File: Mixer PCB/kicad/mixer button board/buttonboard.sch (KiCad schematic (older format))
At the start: 51 parts, among them J1 Conn_01x02, J2 Conn_02x13_Odd_Even, J3 Conn_01x11, sw1 cherry_sk6812, sw10 cherry_sk6812, sw11 cherry_sk6812, sw12 cherry_sk6812, sw13 cherry_sk6812, sw14 cherry_sk6812, sw15 cherry_sk6812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

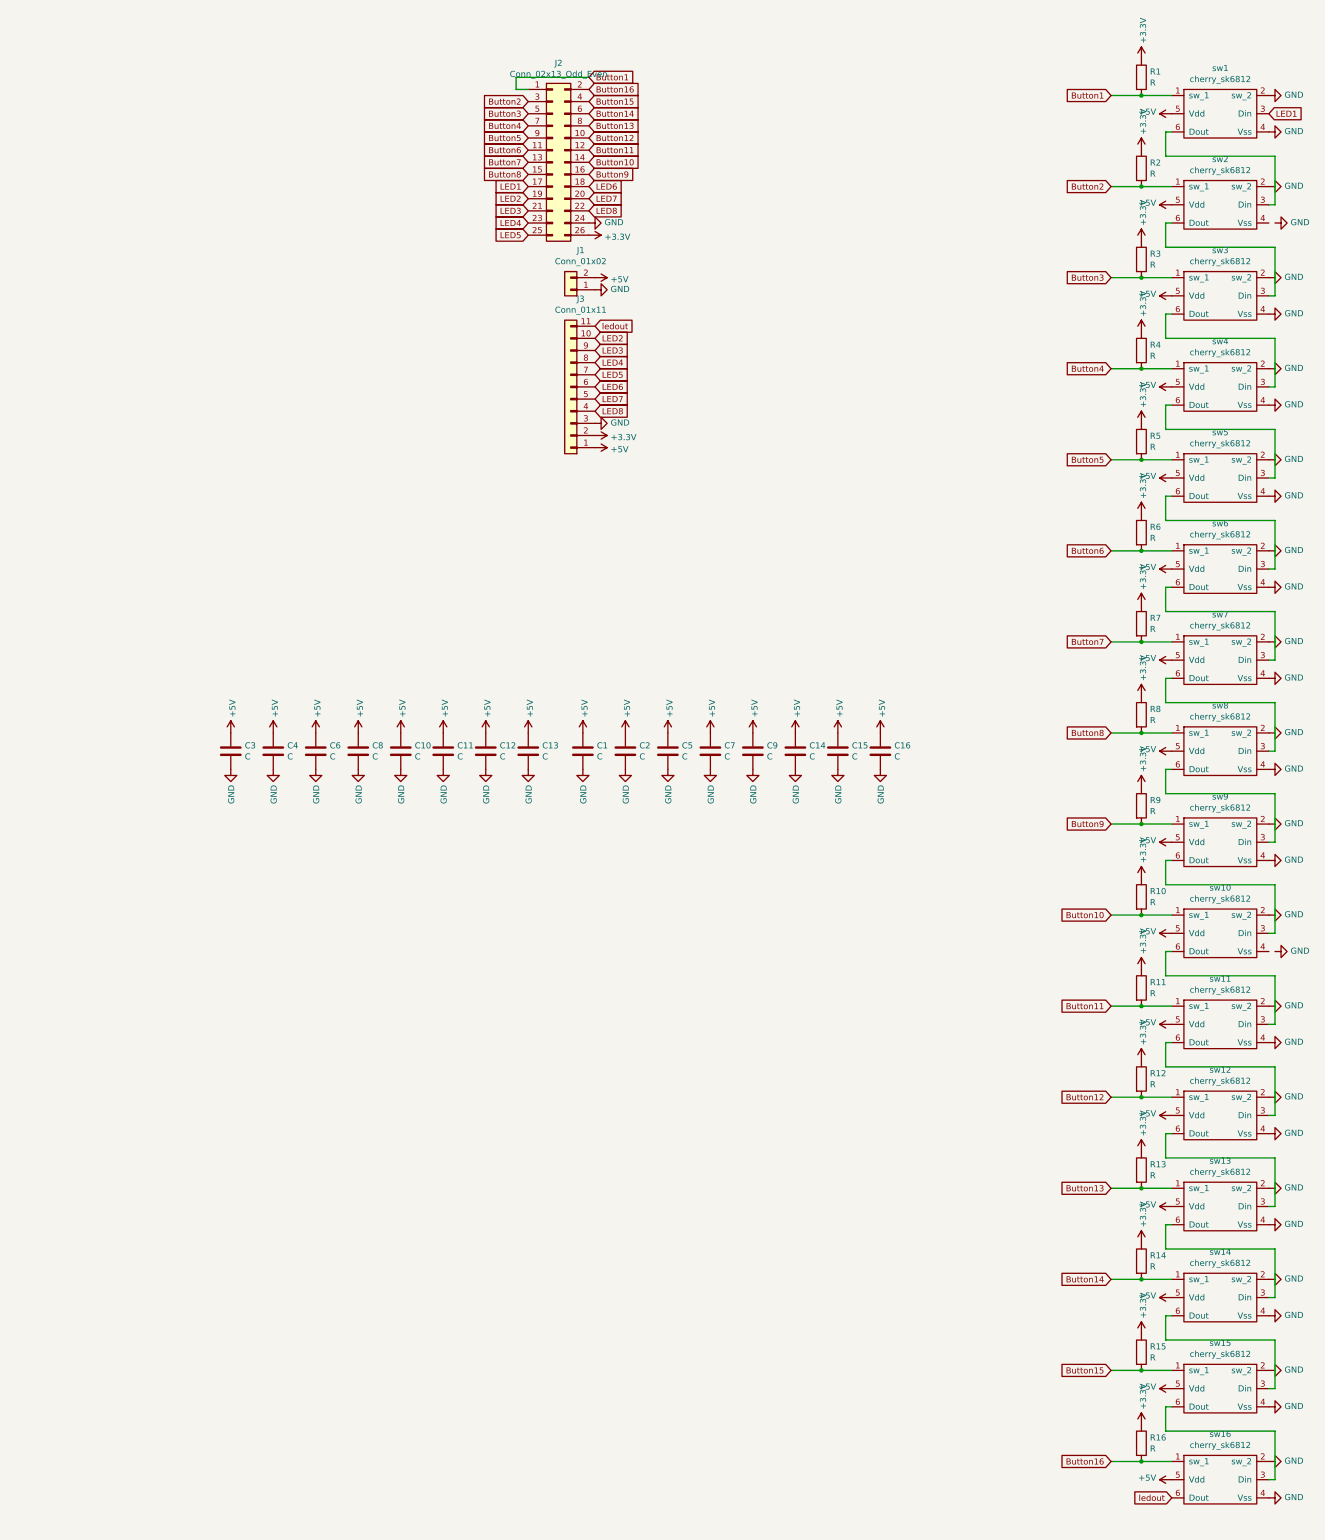
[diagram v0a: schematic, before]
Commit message: Updated Button board to I2C
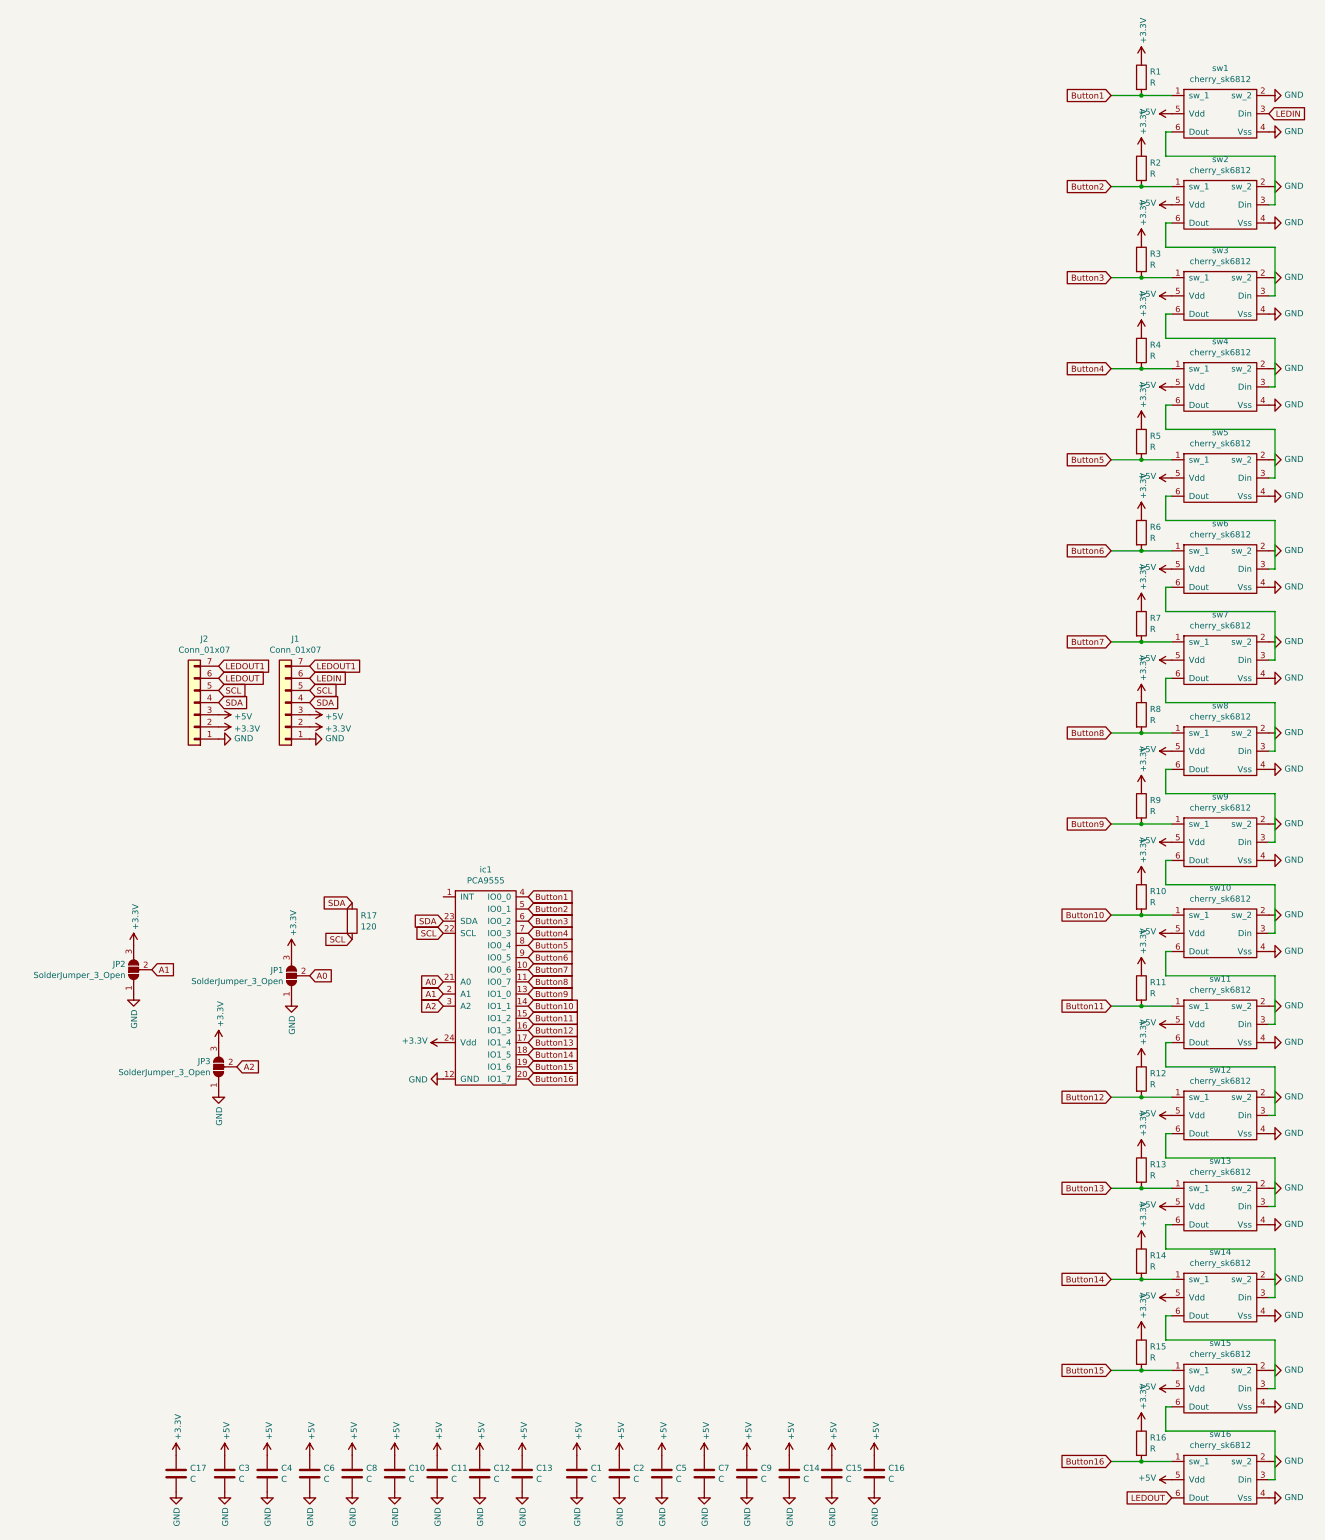
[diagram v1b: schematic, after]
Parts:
- removed J1: Conn_01x02, Connector_PinHeader_2.54mm:PinHeader_1x02_P2.54mm_Vertical, symbol Connector_Generic:Conn_01x02
- removed J2: Conn_02x13_Odd_Even, Connector_PinSocket_2.54mm:PinSocket_2x13_P2.54mm_Vertical, symbol Connector_Generic:Conn_02x13_Odd_Even
- removed J3: Conn_01x11, Connector_PinHeader_2.54mm:PinHeader_1x11_P2.54mm_Vertical, symbol Connector_Generic:Conn_01x11
- added C17: C, Capacitor_SMD:C_0805_2012Metric_Pad1.15x1.40mm_HandSolder, symbol Device:C
- added J1, J2: Conn_01x07, Connector_PinSocket_2.54mm:PinSocket_1x07_P2.54mm_Vertical, symbol Connector_Generic:Conn_01x07
- added JP1, JP2, JP3: SolderJumper_3_Open, Jumper:SolderJumper-3_P1.3mm_Open_RoundedPad1.0x1.5mm, symbol Jumper:SolderJumper_3_Open
- added R17: 120, Resistor_SMD:R_0805_2012Metric_Pad1.15x1.40mm_HandSolder, symbol Device:R
- added ic1: PCA9555, Package_SO:TSSOP-24_4.4x7.8mm_P0.65mm, symbol Kicad_custom:PCA9555
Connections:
- net +3V3: now also C17.1, J1.2 (Pin_2), J2.2 (Pin_2), JP1.3 (B), JP2.3 (B), JP3.3 (B), ic1.24 (Vdd)
- net +5V: now also J1.3 (Pin_3), J2.3 (Pin_3)
- net Button1: now also ic1.4 (IO0_0)
- net Button10: now also ic1.14 (IO1_1)
- net Button11: now also ic1.15 (IO1_2)
- net Button12: now also ic1.16 (IO1_3)
- net Button13: now also ic1.17 (IO1_4)
- net Button14: now also ic1.18 (IO1_5)
- net Button15: now also ic1.19 (IO1_6)
- net Button16: now also ic1.20 (IO1_7)
- net Button2: now also ic1.5 (IO0_1)
- net Button3: now also ic1.6 (IO0_2)
- net Button4: now also ic1.7 (IO0_3)
- net Button5: now also ic1.8 (IO0_4)
- net Button6: now also ic1.9 (IO0_5)
- net Button7: now also ic1.10 (IO0_6)
- net Button8: now also ic1.11 (IO0_7)
- net Button9: now also ic1.13 (IO1_0)
- net GND: now also sw10.4 (Vss), sw2.4 (Vss), C17.2, J1.1 (Pin_1), J2.1 (Pin_1), JP1.1 (A), JP2.1 (A), JP3.1 (A), ic1.12 (GND)
- net LED1 renamed LEDIN
- net LEDIN: now also J1.6 (Pin_6)
- net ledout renamed LEDOUT
- net LEDOUT: now also J2.6 (Pin_6)
- new net A0: JP1.2 (C), ic1.21 (A0)
- new net A1: JP2.2 (C), ic1.2 (A1)
- new net A2: JP3.2 (C), ic1.3 (A2)
- new net LEDOUT1: J1.7 (Pin_7), J2.7 (Pin_7)
- new net SCL: J1.5 (Pin_5), J2.5 (Pin_5), R17.2, ic1.22 (SCL)
- new net SDA: J1.4 (Pin_4), J2.4 (Pin_4), R17.1, ic1.23 (SDA)
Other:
- moved on the sheet: C1, C10, C11, C12, C13, C14, C15, C16, C2, C3, C4, C5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
